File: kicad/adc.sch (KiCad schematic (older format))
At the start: 6 parts, among them U401 TMS320F28388DZWTS

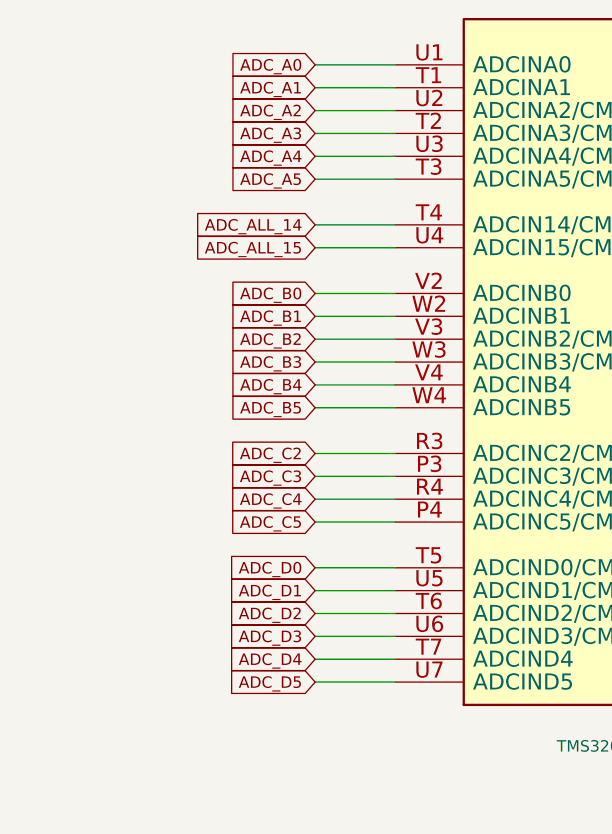
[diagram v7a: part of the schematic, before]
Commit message: I've connected interfaces to gpio and change some muxes
I've changed some muxes reading the datasheet to group same kind of
signals, now it's time to add encoders input
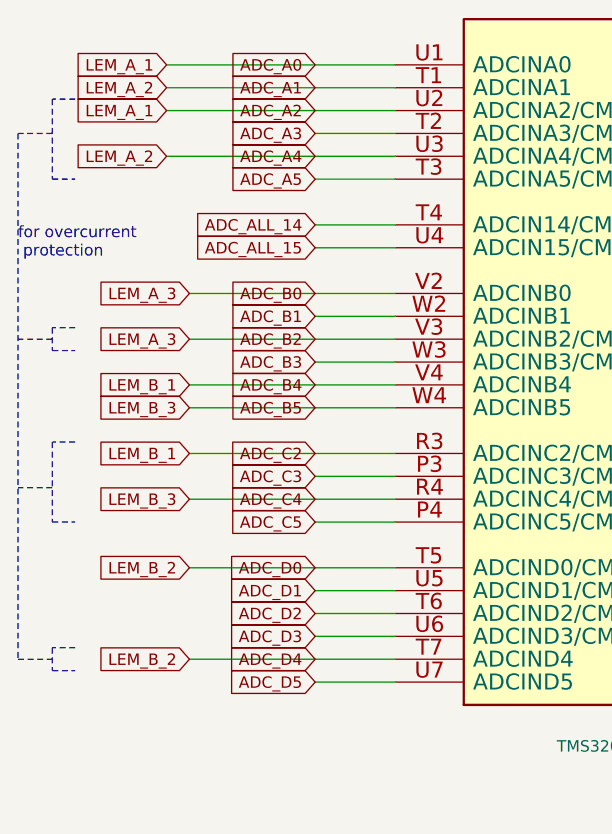
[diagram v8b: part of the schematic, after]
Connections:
- net ADC_A2 is gone; now on net ADC_A0: U401.U2 (ADCINA2/CMPIN1P)
- net ADC_A4 is gone; now on net ADC_A1: U401.U3 (ADCINA4/CMPIN2P)
- net ADC_B2 is gone; now on net ADC_B0: U401.V3 (ADCINB2/CMPIN3P)
- net ADC_C2 is gone; now on net ADC_B4: U401.R3 (ADCINC2/CMPIN6P)
- net ADC_C4 is gone; now on net ADC_B5: U401.R4 (ADCINC4/CMPIN5P)
- net ADC_D4 is gone; now on net ADC_D0: U401.T7 (ADCIND4)
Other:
- note added: "for overcurrent\n protection"
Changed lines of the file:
@@
 	2000 3900 2350 3900
-Wire Wire Line
-	2000 3800 2350 3800
 Wire Wire Line
 	2000 3700 2350 3700
@@
 	2000 3500 2350 3500
 Wire Wire Line
-	2000 3400 2350 3400
-Wire Wire Line
 	2000 3200 2350 3200
-Wire Wire Line
-	2000 3100 2350 3100
 Wire Wire Line
 	2000 3000 2350 3000
 Wire Wire Line
-	2000 2900 2350 2900
-Wire Wire Line
-	2000 2700 2350 2700
-Wire Wire Line
-	2000 2600 2350 2600
-Wire Wire Line
 	2000 2500 2350 2500
 Wire Wire Line
-	2000 2400 2350 2400
-Wire Wire Line
 	2000 2300 2350 2300
-Wire Wire Line
-	2000 2200 2350 2200
 Wire Wire Line
 	2000 2000 2350 2000
 Wire Wire Line
 	2000 1900 2350 1900
-Wire Wire Line
-	2000 1700 2350 1700
-Wire Wire Line
-	2000 1600 2350 1600
-Wire Wire Line
-	2000 1500 2350 1500
-Wire Wire Line
-	2000 1400 2350 1400
-Wire Wire Line
-	2000 1300 2350 1300
-Wire Wire Line
-	2000 1200 2350 1200
 Text GLabel 2000 1200 0    50   Input ~ 0
 ADC_A0
@@
 Text GLabel 2000 3900 0    50   Input ~ 0
 ADC_D5
+Text GLabel 1350 1300 0    50   Input ~ 0
+LEM_A_2
+Text GLabel 1350 1200 0    50   Input ~ 0
+LEM_A_1
+Wire Wire Line
+	1350 1200 2350 1200
+Wire Wire Line
+	1350 1300 2350 1300
+Wire Wire Line
+	1350 1400 2350 1400
+Wire Wire Line
+	1350 1600 2350 1600
+Text GLabel 1450 2200 0    50   Input ~ 0
+LEM_A_3
+Text GLabel 1450 3800 0    50   Input ~ 0
+LEM_B_2
+Text GLabel 1450 2600 0    50   Input ~ 0
+LEM_B_1
+Text GLabel 1450 2700 0    50   Input ~ 0
+LEM_B_3
+Text GLabel 1350 1400 0    50   Input ~ 0
+LEM_A_1
+Text GLabel 1350 1600 0    50   Input ~ 0
+LEM_A_2
+Text GLabel 1450 2400 0    50   Input ~ 0
+LEM_A_3
+Wire Wire Line
+	2350 1500 2000 1500
+Wire Wire Line
+	2350 1700 2000 1700
+Wire Wire Line
+	1450 2200 2350 2200
+Wire Wire Line
+	1450 2400 2350 2400
+Text GLabel 1450 2900 0    50   Input ~ 0
+LEM_B_1
+Text GLabel 1450 3100 0    50   Input ~ 0
+LEM_B_3
+Text GLabel 1450 3400 0    50   Input ~ 0
+LEM_B_2
+Wire Wire Line
+	1450 3400 2350 3400
+Wire Wire Line
+	1450 3800 2350 3800
+Wire Wire Line
+	1450 3100 2350 3100
+Wire Wire Line
+	1450 2900 2350 2900
+Wire Wire Line
+	1450 2700 2350 2700
+Wire Wire Line
+	1450 2600 2350 2600
+Wire Notes Line style solid
+	950  1350 850  1350
+Wire Notes Line style solid
+	850  1350 850  1700
+Wire Notes Line style solid
+	850  1700 950  1700
+Wire Notes Line style solid
+	950  2350 850  2350
+Wire Notes Line style solid
+	850  2350 850  2450
+Wire Notes Line style solid
+	850  2450 950  2450
+Wire Notes Line style solid
+	950  2850 850  2850
+Wire Notes Line style solid
+	850  2850 850  3200
+Wire Notes Line style solid
+	850  3200 950  3200
+Wire Notes Line style solid
+	950  3750 850  3750
+Wire Notes Line style solid
+	850  3750 850  3850
+Wire Notes Line style solid
+	850  3850 950  3850
+Wire Notes Line style solid
+	700  1500 700  3800
+Wire Notes Line style solid
+	700  3800 850  3800
+Wire Notes Line style solid
+	850  3050 700  3050
+Wire Notes Line
+	850  1500 700  1500
+Wire Notes Line style solid
+	850  2400 700  2400
+Text Notes 700  2050 0    50   ~ 0
+for overcurrent\n protection
 $EndSCHEMATC
